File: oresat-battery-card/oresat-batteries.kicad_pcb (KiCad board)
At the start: 4 copper layers, 99.8 x 94.6 mm, 340 parts, among them J1 J-SAMTEC-TFM-120-X1-XXX-D-RA, J2 SM14B-SHLS-TF, Q1 DMP2240UDM-7, Q13 SI7111EDN-T1-GE3, Q14 DMP2035UQ-7, Q15 DMP2035UQ-7, Q16 SI7111EDN-T1-GE3, Q17 SI7111EDN-T1-GE3, Q18 SI7111EDN-T1-GE3, Q19 SI7111EDN-T1-GE3, Q2 DMN2053UQ-13, Q20 DMN2053UQ-13, Q21 DMN2053UQ-13, Q22 SQS484ENW-T1_GE3, Q23 DMP2035UQ-7, Q24 DMN2053UQ-13, Q25 DMN2053UQ-13, Q26 DMN2053UQ-13, Q27 DMN2053UQ-13, Q29 SQS484ENW-T1_GE3, Q3 DMP3050LVTQ-7, Q31 SI7111EDN-T1-GE3, Q32 DMP2035UQ-7, Q33 DMP2035UQ-7, Q34 SI7111EDN-T1-GE3, Q35 SI7111EDN-T1-GE3, Q36 SI7111EDN-T1-GE3, Q37 SI7111EDN-T1-GE3, Q38 DMN2053UQ-13, Q39 DMN2053UQ-13, Q4 DMP3050LVTQ-7, Q40 DMP2035UQ-7, Q42 DMP2240UDM-7, Q43 DMP2240UDM-7, Q44 DMN2053UQ-13, Q5 DMN2053UQ-13, Q6 DMN2053UQ-13, Q7 DMN2053UQ-13, Q8 DMN2053UQ-13, Q9 DMN2053UQ-13, SW1 D2F-L3-D3 (LEFT), SW2 D2F-L3-D3 (RIGHT), SW3 D2F-L3-D3 (LEFT), SW4 D2F-L3-D3 (RIGHT), U1 MAX7310, U10 TPS259830ONRGER, U11 LTC4412, U12 MAX17205G, U13 S-8209AAA-T8T1U, U14 S-8209AAA-T8T1U, U15 TPS259830ONRGER, U16 LTC4412, U17 MAX17205G, U2 MIC842LYC5, U20 TCAN330G, U3 MIC842LYC5, U4 MAX4211, U5 TPS62111RSA, U6 TS5A21366DCUR, U7 MCXN947VKLT, U8 S-8209AAA-T8T1U, U9 S-8209AAA-T8T1U, Y2 24 MHz

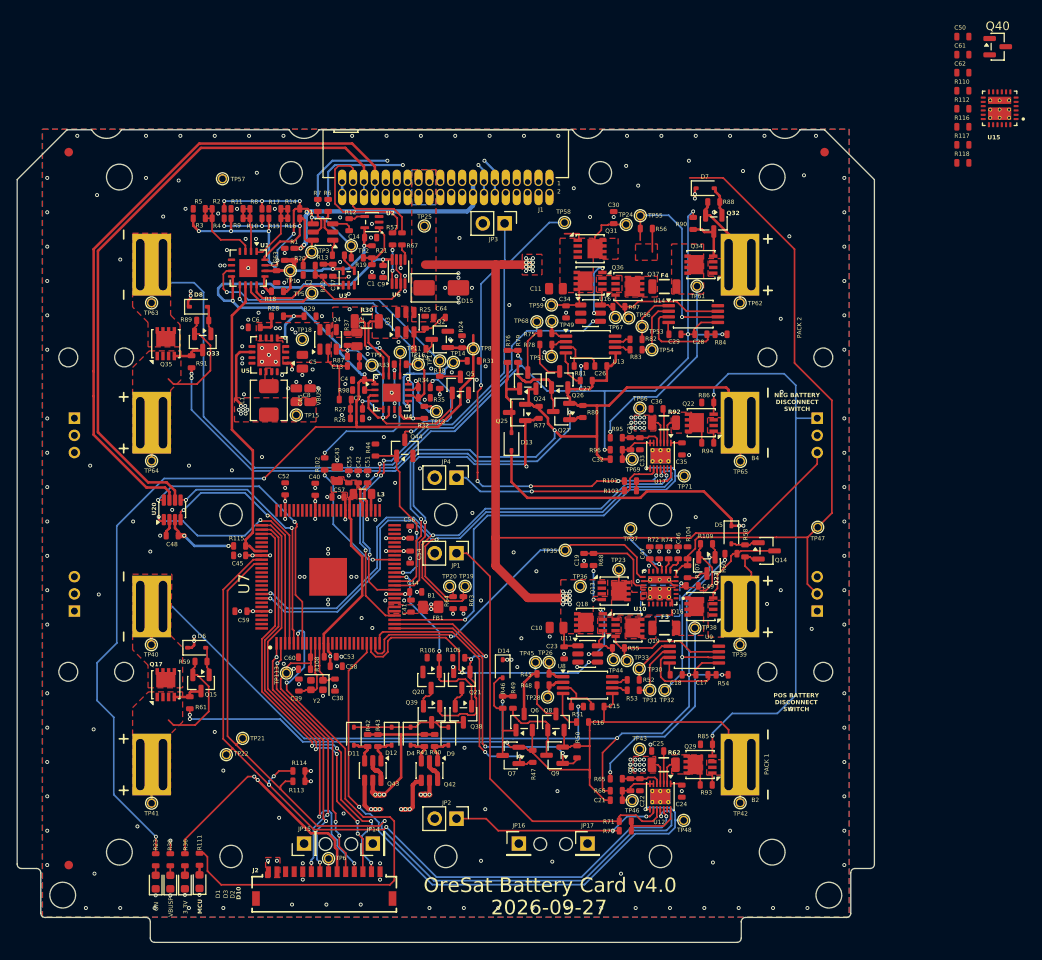
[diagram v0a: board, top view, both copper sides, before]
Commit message: Battery Card 4.0, no ERC or DRC errors or warnings
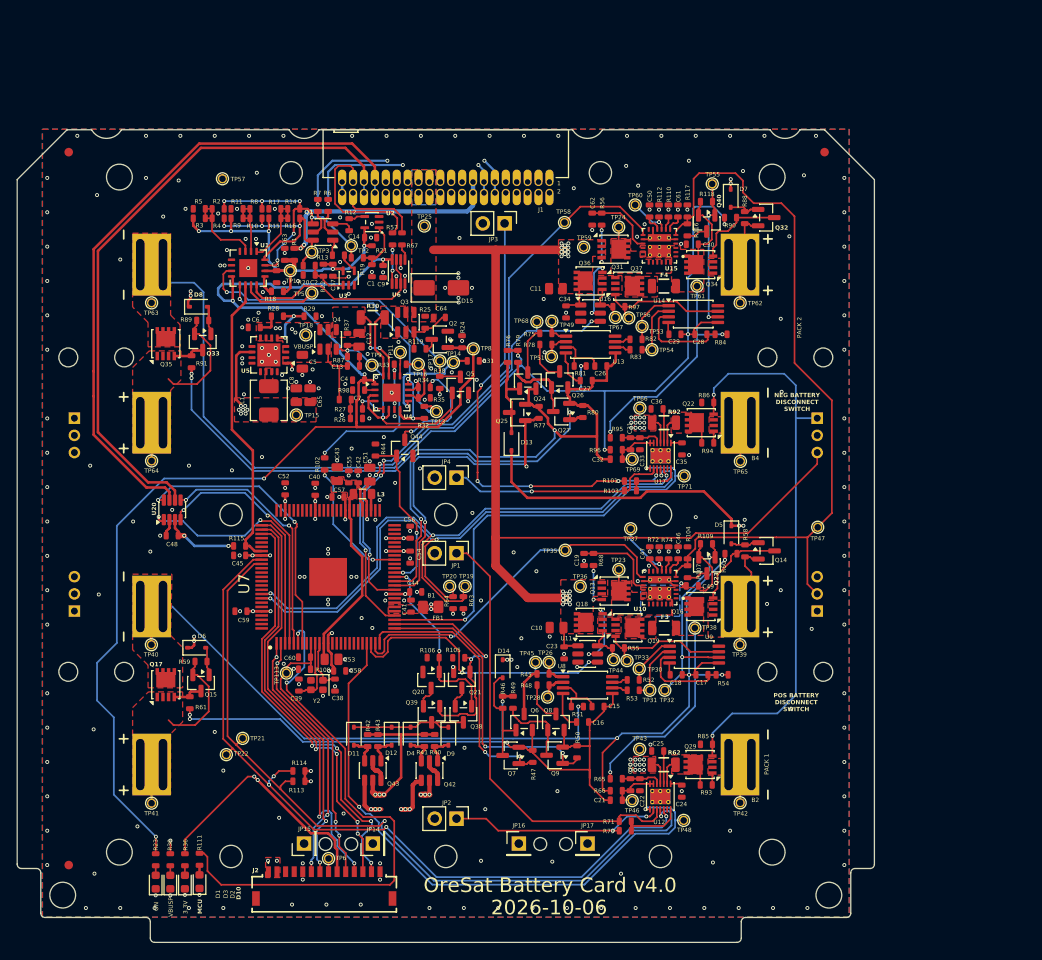
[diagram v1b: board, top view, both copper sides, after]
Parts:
- added TP60: TEST-POINT-LARGE-SQUARE, oresat-misc:TestPoint-0.75mm-th, F.Cu at (170.6, 66.5)
- C51, C53: footprint oresat-passives:0603-C-NOSILK -> oresat-passives:0805-C-NOSILK
- R107: value 357K -> 357k
- R110: value 210 -> 154
- R112: value 210 -> 1k
- R116: value 100k -> 357k
- R56: value 100k -> 2
- moved C62 46.4 mm to (165.6, 68.1), turned to -90 degrees
- moved U15 42.7 mm to (173.4, 71.2)
- moved C50 41.7 mm to (172.2, 67.2), turned to 90 degrees
- moved Q40 39.6 mm to (178.9, 68.6), turned to -90 degrees
- moved C61 37.8 mm to (175.5, 67.2), turned to 90 degrees
- moved R112 37.3 mm to (173.3, 67.2), turned to 90 degrees
- moved R110 37.0 mm to (174.4, 67.2), turned to 90 degrees
- moved R116 34.2 mm to (176.6, 69.3), turned to -90 degrees
- moved R117 33.0 mm to (176.6, 67.2), turned to -90 degrees
- moved R118 30.2 mm to (178.8, 66.1), turned to 180 degrees
- moved C30 9.66 mm to (177.2, 71.0), turned to 180 degrees
- moved TP55 9.16 mm to (179.5, 64.0)
- moved TP59 7.70 mm to (164.6, 71.4)
- moved Q32 6.14 mm to (185.8, 67.9), turned to 0 degrees
- moved R56 5.32 mm to (166.7, 68.1), turned to -90 degrees
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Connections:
- B2 pad 2: /Battery Pack 1 (BOTTOM)/BATTNEG-PK1 -> Net-(B2--)
- Q29 pad 1: /Battery Pack 1 (BOTTOM)/BATTNEG-PK1 -> Net-(B2--)
- Q29 pad 2: /Battery Pack 1 (BOTTOM)/BATTNEG-PK1 -> Net-(B2--)
- Q29 pad 3: /Battery Pack 1 (BOTTOM)/BATTNEG-PK1 -> Net-(B2--)
- R93 pad 2: /Battery Pack 1 (BOTTOM)/BATTNEG-PK1 -> Net-(B2--)
- TP42 pad 1: /Battery Pack 1 (BOTTOM)/BATTNEG-PK1 -> Net-(B2--)
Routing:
- net /Battery Pack 1 (BOTTOM)/BATTNEG-PK1: track 106.9 -> 75.8 mm
- net /Battery Pack 2 (TOP)/BATTNEG-PK2: track 113.2 -> 88.0 mm
- net /INH-POS-BATT-DISC: track 78.0 -> 89.1 mm
- net /Battery Pack 2 (TOP)/DCHG-STAT-OC-PK2: track 58.5 -> 69.1 mm
- net /Battery Pack 2 (TOP)/VBATT-PK2: track 26.8 -> 36.6 mm
- net Net-(U15-DVDT/BGATE): track 0.00 -> 8.29 mm
- net Net-(B2--): track 0.00 -> 7.62 mm
- net /~{SHUTDOWN}: track 309.6 -> 303.0 mm
- net (no net): track 5.98 -> 0.00 mm
- net /Battery Pack 2 (TOP)/~{DISCHARGE-PK2}: track 23.0 -> 17.5 mm, vias 1 -> 2
- net /Battery Pack 2 (TOP)/INTERCELL-PK2: track 126.4 -> 131.8 mm
- net Net-(Q32-D): track 5.37 -> 10.6 mm
- net Net-(U15-IMON): track 0.00 -> 5.19 mm, vias 0 -> 1
- net Net-(B4--): track 6.44 -> 11.5 mm
- net +3.3V: track 83.2 -> 86.9 mm, vias 36 -> 38
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- added copper zone on F.Cu, net Net-(B2--)
- added copper zone on F.Cu, net Net-(B4--)
- removed copper zone on F.Cu, net /Battery Pack 1 (BOTTOM)/BATTNEG-PK1
- removed copper zone on F.Cu, net /Battery Pack 2 (TOP)/BATTNEG-PK2
- removed copper zone on F.Cu, net Net-(Q31-G)
